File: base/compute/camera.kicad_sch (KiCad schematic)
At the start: 9 parts, among them J2 Conn_01x20

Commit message: schema  extension finished, pre  merge
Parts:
- C17, C20: farnell# 3013485 -> 3010126; manf# CL21B106KOQNNNE -> CL21A106KAYNNNE; mouser# 187-CL21B106KOQNNNE -> 187-CL21A106KAYNNNE
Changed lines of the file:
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@@
 			)
 		)
-		(property "manf#" "CL21B106KOQNNNE"
+		(property "manf#" "CL21A106KAYNNNE"
 			(at 203.2 63.5 0)
 			(hide yes)
@@
 			)
 		)
-		(property "farnell#" "3013485"
+		(property "farnell#" "3010126"
 			(at 203.2 63.5 0)
 			(hide yes)
@@
 			)
 		)
-		(property "mouser#" "187-CL21B106KOQNNNE"
+		(property "mouser#" "187-CL21A106KAYNNNE"
 			(at 203.2 63.5 0)
 			(hide yes)
@@
 			)
 		)
-		(property "manf#" "CL21B106KOQNNNE"
+		(property "manf#" "CL21A106KAYNNNE"
 			(at 179.07 119.38 0)
 			(hide yes)
@@
 			)
 		)
-		(property "farnell#" "3013485"
+		(property "farnell#" "3010126"
 			(at 179.07 119.38 0)
 			(hide yes)
@@
 			)
 		)
-		(property "mouser#" "187-CL21B106KOQNNNE"
+		(property "mouser#" "187-CL21A106KAYNNNE"
 			(at 179.07 119.38 0)
 			(hide yes)

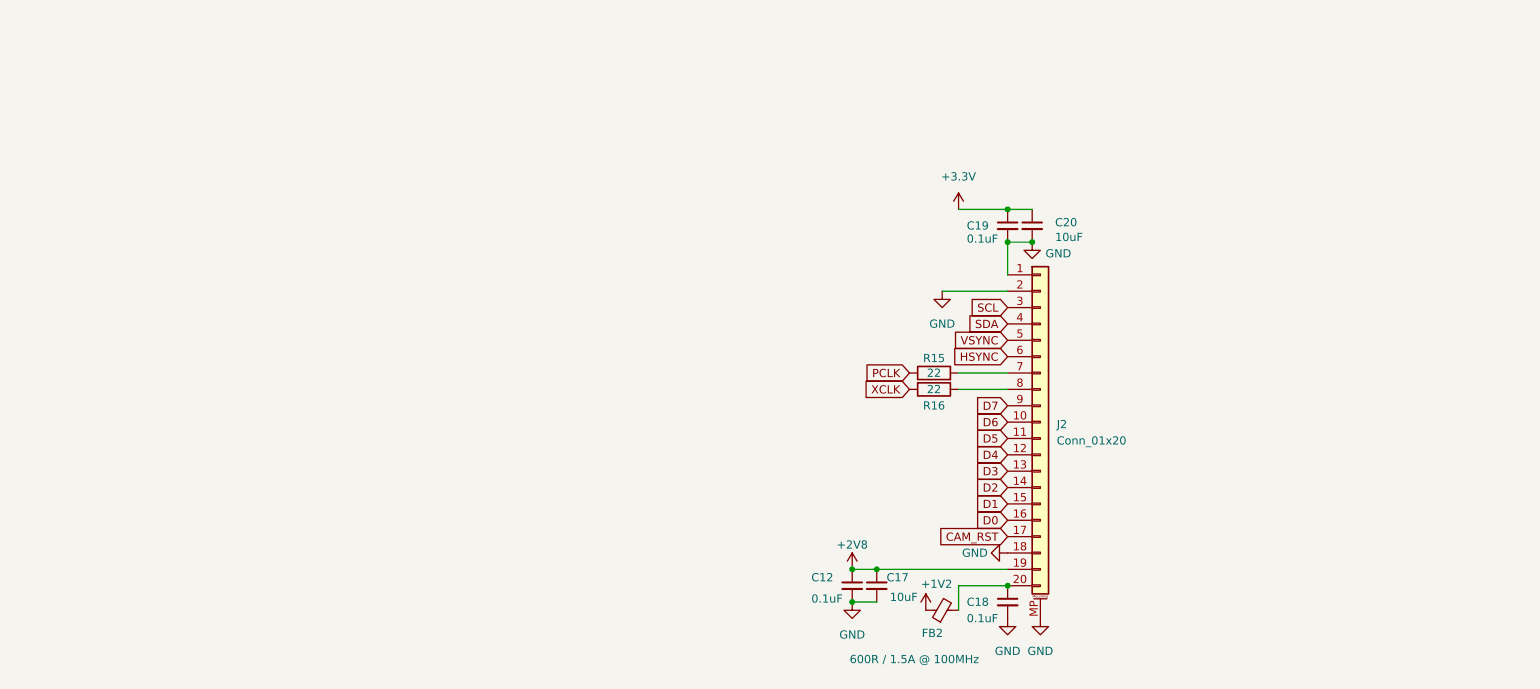
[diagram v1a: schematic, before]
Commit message: schema support spindle, fan , 24V, compliant with VEVOR
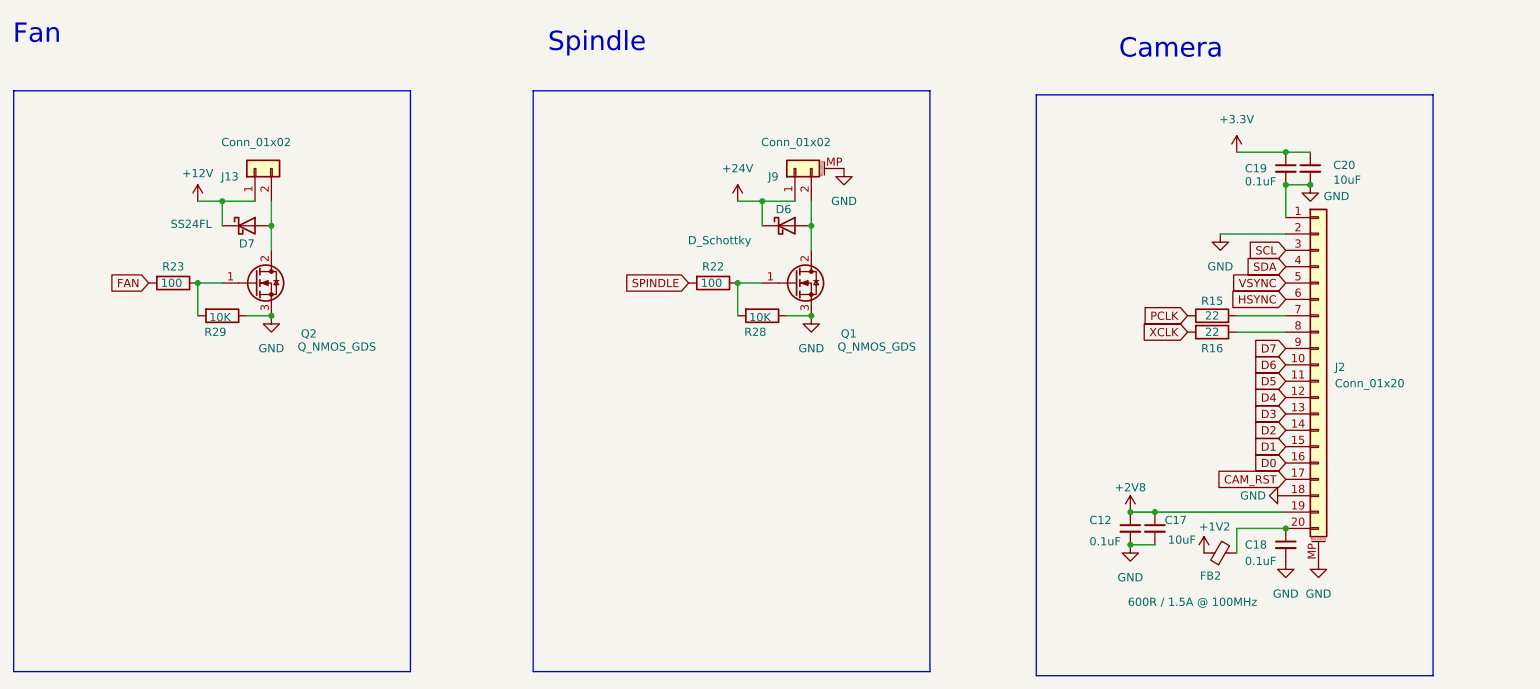
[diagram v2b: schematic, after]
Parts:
- added D6: D_Schottky, Diode_SMD:D_SMA, symbol Device:D_Schottky
- added D7: SS24FL, Diode_SMD:D_SMA, symbol Diode:SS24
- added J13: Conn_01x02, footprints:TSM-102-01-L-SV, symbol Connector_Generic:Conn_01x02
- added J9: Conn_01x02, footprints:21548291, symbol Connector_Generic_MountingPin:Conn_01x02_MountingPin
- added Q1: Q_NMOS_GDS, Package_TO_SOT_SMD:TO-252-2, symbol Transistor_FET:Q_NMOS_GDS
- added Q2: Q_NMOS_GDS, Package_TO_SOT_SMD:SOT-23, symbol Transistor_FET:Q_NMOS_GDS
- added R22, R23: 100, Resistor_SMD:R_0805_2012Metric_Pad1.20x1.40mm_HandSolder, symbol Device:R
- added R28, R29: 10K, Resistor_SMD:R_0805_2012Metric, symbol Device:R
- C17, C20: farnell# 3010126 -> 3790440; manf# CL21A106KAYNNNE -> GRM21BR61H106KE43L; mouser# 187-CL21A106KAYNNNE -> 81-GRM21BR61H106KE3L
- R15, R16: farnell# 2303365 -> 1652962; manf# ERJ-6ENF22R0V -> CRCW080522R0FKEA; mouser# 667-ERJ-6ENF22R0V -> 71-CRCW0805-22-E3
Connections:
- net GND: now also J9.MP (MountPin), Q1.3 (S), Q2.3 (S), R28.1, R29.1
- new net: Q1.1 (G), R22.1, R28.2
- new net: D6.2 (A), J9.2 (Pin_2), Q1.2 (D)
- new net: Q2.1 (G), R23.1, R29.2
- new net: D7.2 (A), J13.2 (Pin_2), Q2.2 (D)
- new net +12V: D7.1 (K), J13.1 (Pin_1)
- new net +24V: D6.1 (K), J9.1 (Pin_1)
- new net FAN: R23.2
- new net SPINDLE: R22.2
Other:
- note added: "Camera"
- note added: "Fan"
- note added: "Spindle"
- moved on the sheet: C12, C17, C18, C19, C20, FB2, J2, R15, R16

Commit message: board passes all tests
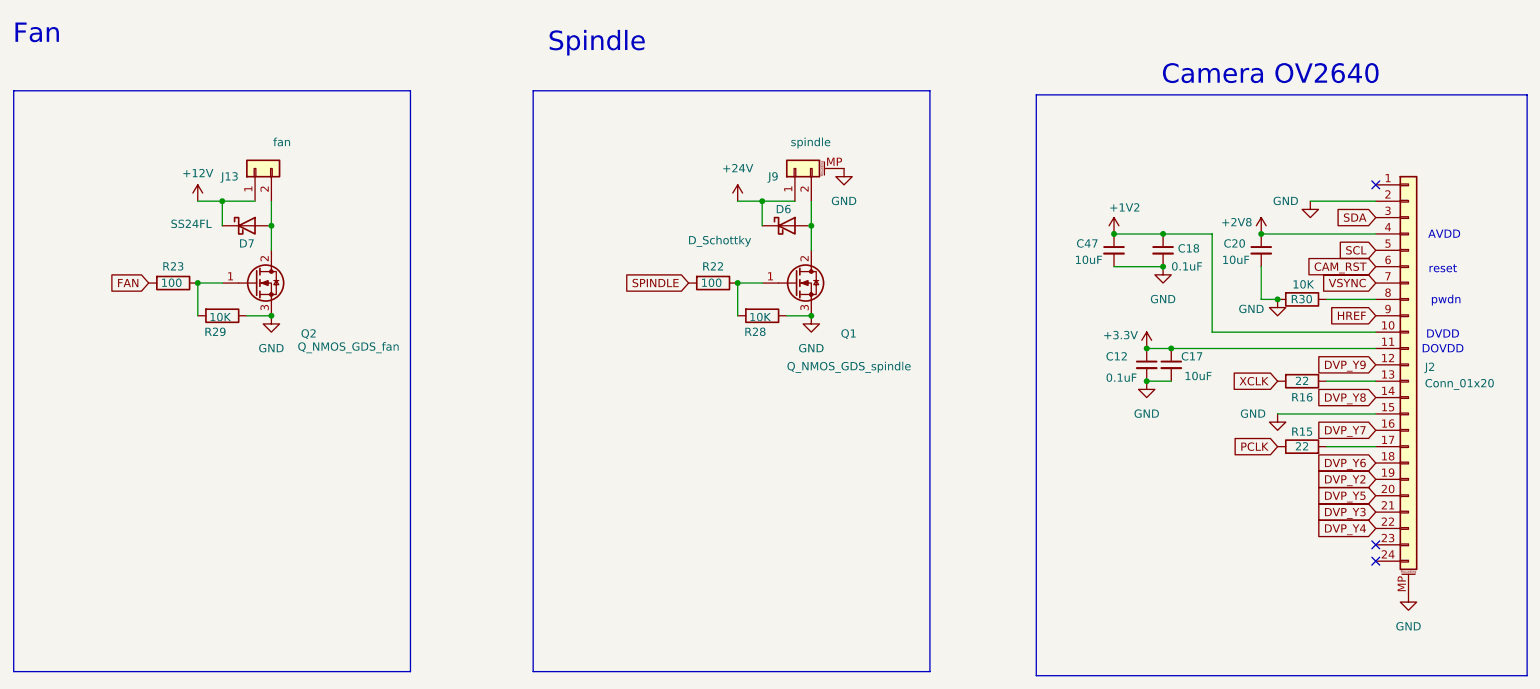
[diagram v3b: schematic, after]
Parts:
- removed C19: 0.1uF, Capacitor_SMD:C_0805_2012Metric_Pad1.18x1.45mm_HandSolder, symbol Device:C_Small
- removed FB2: 600R / 1.5A @ 100MHz, Inductor_SMD:L_0805_2012Metric, symbol Device:FerriteBead_Small
- added C47: 10uF, Capacitor_SMD:C_0805_2012Metric_Pad1.18x1.45mm_HandSolder, symbol Device:C_Small
- added R30: 10K, Resistor_SMD:R_0805_2012Metric, symbol Device:R
- J13: value Conn_01x02 -> fan
- J2: footprint footprints:CON_527452097_MOL -> Connector_FFC-FPC:Hirose_FH12-24S-0.5SH_1x24-1MP_P0.50mm_Horizontal; symbol Connector_Generic_MountingPin:Conn_01x20_MountingPin -> Connector_Generic_MountingPin:Conn_01x24_MountingPin; farnell# 1827155 -> 1324552; manf# 52745-2097 -> FH12-24S-0.5SH(55); mouser# 538-52745-2097 -> 798-FH12-24S-0.5SH55; notes (none) -> kan 10 bit uitzenden, maar dat is te veel info; reference1 (none) -> https://dl.espressif.com/dl/schematics/SCH_ESP32-S3-EYE-MB_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; reference2 (none) -> https://www.mpja.com/download/ov2640data%20sheet.pdf
- J9: value Conn_01x02 -> spindle
- Q1: value Q_NMOS_GDS -> Q_NMOS_GDS_spindle
- Q2: value Q_NMOS_GDS -> Q_NMOS_GDS_fan
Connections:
- net D1 is gone; now on net GND: J2.15 (Pin_15)
- net D5 is gone; now on net +3.3V: J2.11 (Pin_11)
- net D6 is gone; now on net +1V2: J2.10 (Pin_10)
- net HSYNC is gone; now on net CAM_RST: J2.6 (Pin_6)
- net +1V2: now also C18.1, C47.1
- net +2V8: now also C20.1, J2.4 (Pin_4); no longer C12.1, C17.1, J2.19 (Pin_19)
- net +3.3V: now also C12.1, C17.1; no longer C20.1
- net CAM_RST: no longer J2.17 (Pin_17)
- net GND: now also C47.2, R30.2; no longer J2.1 (Pin_1), J2.18 (Pin_18)
- net SCL: now also J2.5 (Pin_5); no longer J2.3 (Pin_3)
- net SDA: now also J2.3 (Pin_3); no longer J2.4 (Pin_4)
- net VSYNC: now also J2.7 (Pin_7); no longer J2.5 (Pin_5)
- net DVP_Y5: now reaches J2.20 (Pin_20)
- net DVP_Y5: no longer C18.1
- net at J2.8 (Pin_8): now also R30.1; no longer R16.1
- net at R15.2: now also J2.17 (Pin_17); no longer J2.7 (Pin_7)
- net D0 renamed DVP_Y7
- net D2 renamed DVP_Y8
- net D3: no longer names the net of J2.13 (Pin_13)
- net D3: now also R16.1
- net D4 renamed DVP_Y9
- net D7 renamed HREF
- new net DVP_Y2: J2.19 (Pin_19)
- new net DVP_Y3: J2.21 (Pin_21)
- new net DVP_Y4: J2.22 (Pin_22)
- new net DVP_Y6: J2.18 (Pin_18)
- no-connect marks 0 -> 3
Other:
- note added: "AVDD"
- note added: "Camera OV2640"
- note added: "DOVDD"
- note added: "DVDD"
- note added: "pwdn"
- note added: "reset"
- note removed: "Camera"
- moved on the sheet: C12, C17, C18, C20, R15, R16
